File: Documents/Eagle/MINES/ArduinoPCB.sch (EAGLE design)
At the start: 17 parts, among them IC1 ULN2003AN, IC2 ULN2003AN, X1 B2B-XH-2, X10 B5B-XH-2, X11 B2B-XH-2, X12 B2B-XH-2, X13 B2B-XH-2, X14 B2B-XH-2, X2 B2B-XH-2, X3 B4B-XH-2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

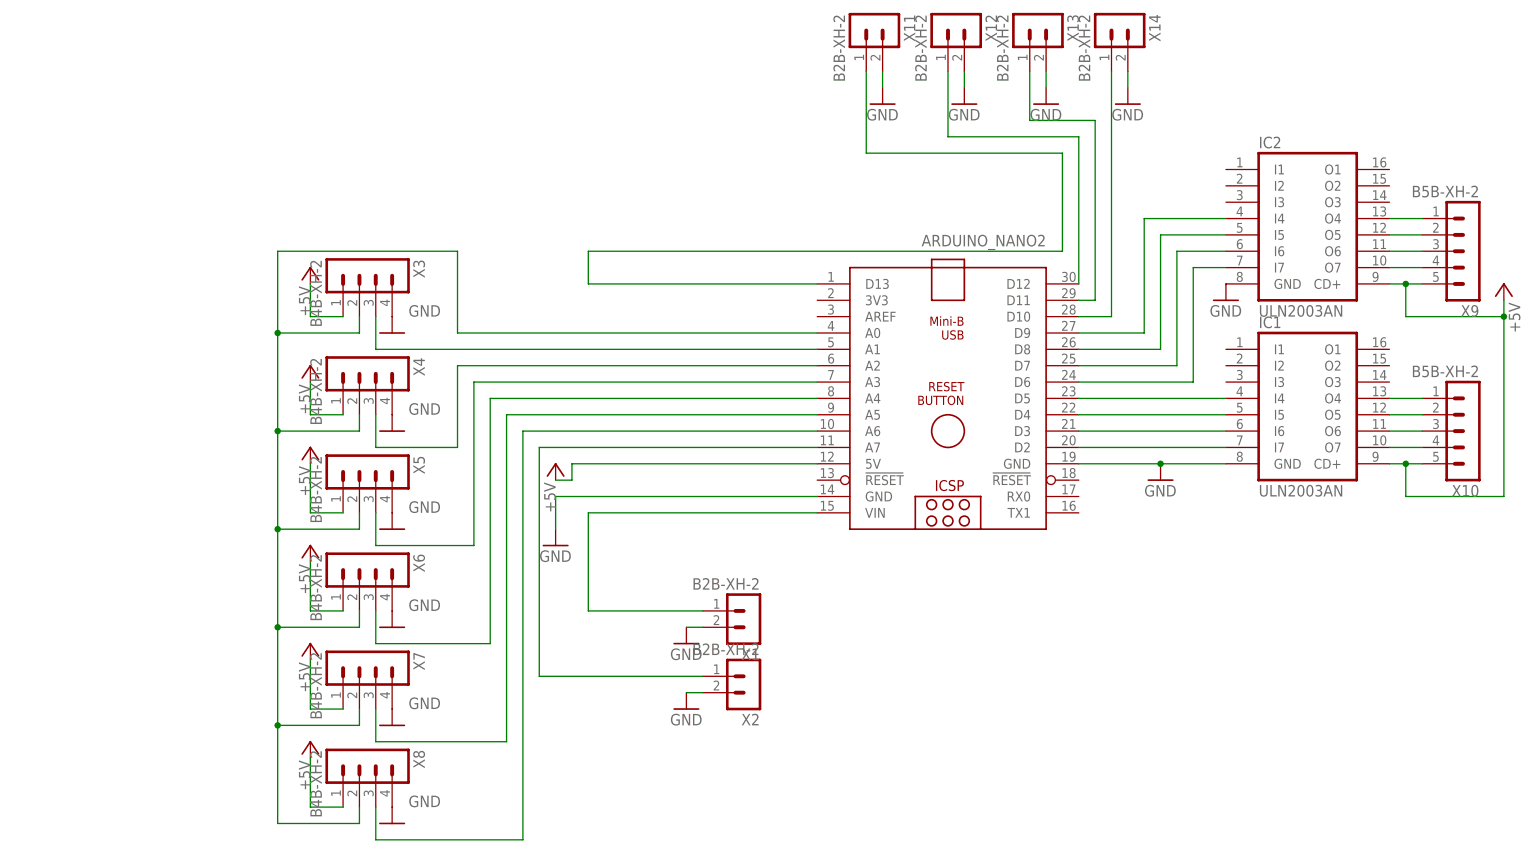
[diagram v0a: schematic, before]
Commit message: Put 2 arduinos in eagle
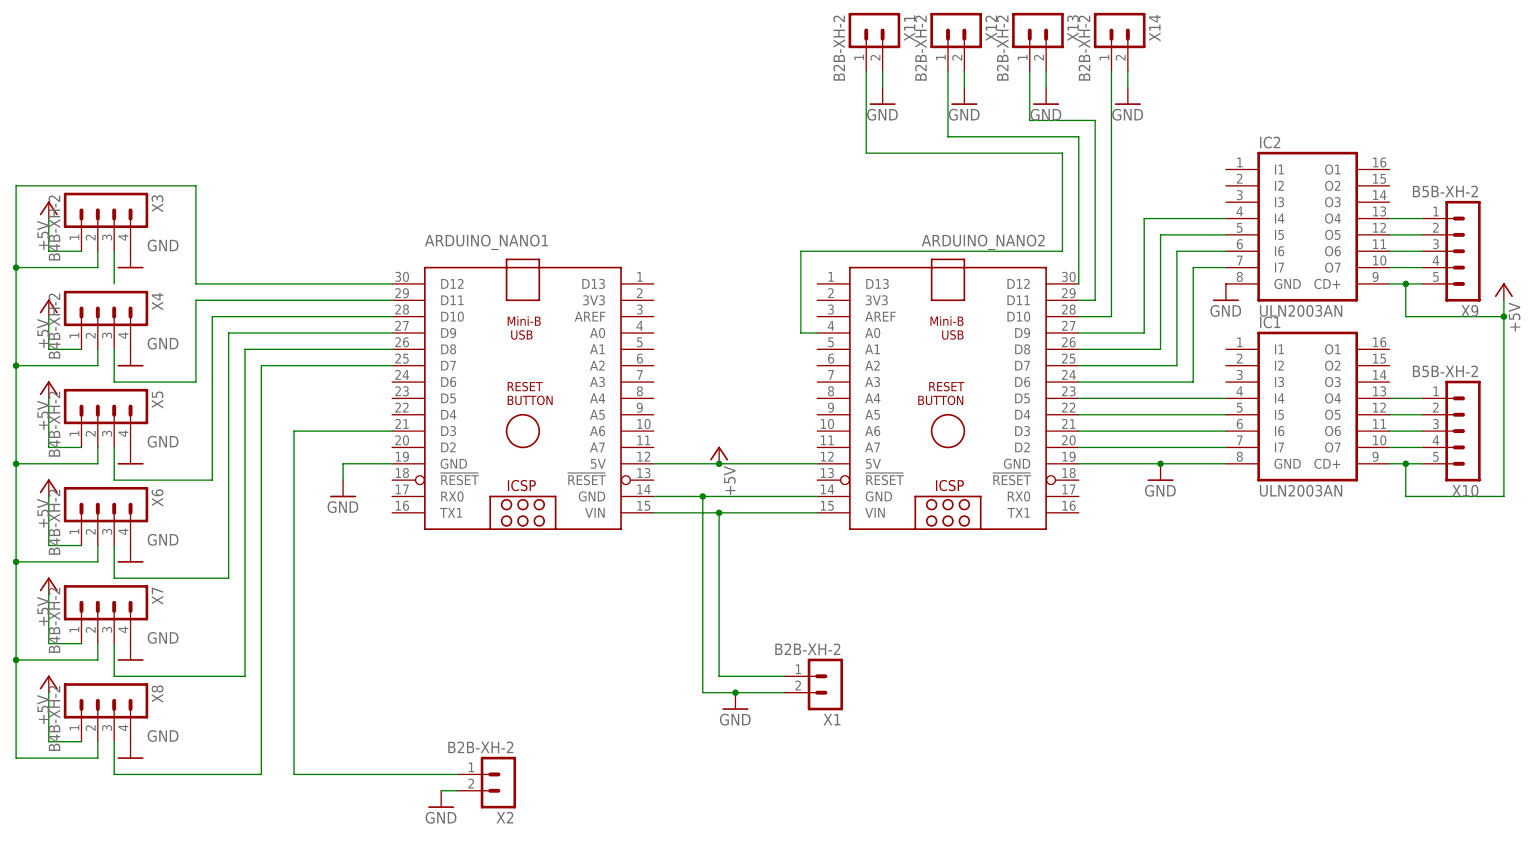
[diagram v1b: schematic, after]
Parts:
- added ARDUINO_NANO1: (no value), ArduinoNanoV31:ARDUINO_NANO
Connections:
- removed net N$21: ARDUINO_NANO2.GND@2
- net +5V: now also ARDUINO_NANO1.5V
- net GND: now also ARDUINO_NANO1.GND@1, ARDUINO_NANO1.GND@2, ARDUINO_NANO2.GND@2
- net N$19: now also ARDUINO_NANO2.A0; no longer ARDUINO_NANO2.D13
- net N$20: now also ARDUINO_NANO1.VIN
- net N$22: now also ARDUINO_NANO1.D3; no longer ARDUINO_NANO2.A7
- net N$24: now also ARDUINO_NANO1.D8; no longer ARDUINO_NANO2.A5
- net N$25: no longer ARDUINO_NANO2.A1
- net N$27: now also ARDUINO_NANO1.D11; no longer ARDUINO_NANO2.A2
- net N$28: now also ARDUINO_NANO1.D10; no longer ARDUINO_NANO2.A3
- net N$31: now also ARDUINO_NANO1.D9; no longer ARDUINO_NANO2.A4
- net N$34: now also ARDUINO_NANO1.D12; no longer ARDUINO_NANO2.A0
- net N$35: now also ARDUINO_NANO1.D7; no longer ARDUINO_NANO2.A6
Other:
- moved on the sheet: X1, X2, X3, X4, X5, X6, X7, X8
